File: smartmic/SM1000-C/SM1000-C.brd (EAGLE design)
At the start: 65 x 90 mm, 182 parts, among them CN1 HDR100-3, CN10 MJ-3523-SMT, CN11 HDR100-3, CN12 DF11-16DS, CN2 MOLEX-MINI-B-SMT, CN3 RASM722PX, CN4 RJ-45, CN5 MJ-3523-SMT, CN6 SJ-3524-SMT, CN7 MJ-3523-SMT, CN8 SJ-3524-SMT, CN9 MJ-3523-SMT, J1 JMP-2PIN, J3 JMP-2PIN, J4 JMP-2PIN, J5 JMP-2PIN, P1 TPAD50, P10 TPAD50, P11 TPAD50, P12 TPAD50, P13 TPAD50, P14 TPAD50, P15 TPAD50, P16 TPAD50, P17 TPAD50, P18 TPAD50, P19 TPAD50, P2 TPAD50, P20 TPAD50, P21 PAD070-035, P22 PAD070-035, P23 PAD070-035, P24 PAD070-035, P3 TPAD50, P4 TPAD50, P5 TPAD50, P6 TPAD50, P7 TPAD50, P8 TPAD50, P9 TPAD50, SW1 SW-BOURNS-7914S, SW2 SW-BOURNS-7914S, SW3 DPDT, SW4 SW-BOURNS-7914S, T1 SM-LP-5001, T2 SM-LP-5001, U1 STM32F405, U2 LD3985M33R, U3 STMPS2141, U4 EMIF02-USB03F2, U5 TPS54329E, U6 LMV341, U7 LMV341, U8 LM386M-1, U9 LMV341

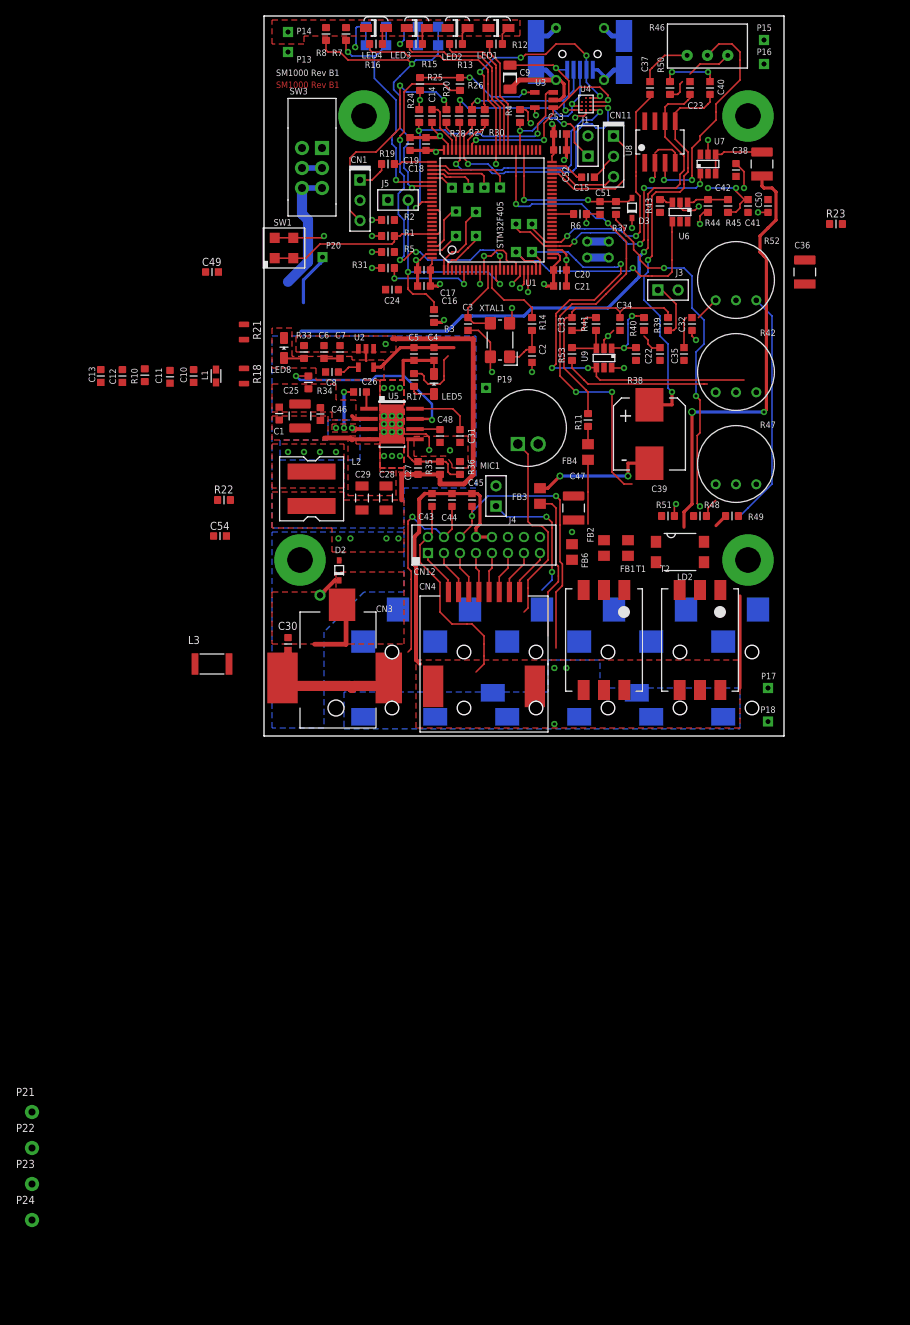
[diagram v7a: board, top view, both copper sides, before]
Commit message: Schematic & PCB changes  RGB 09/24/14
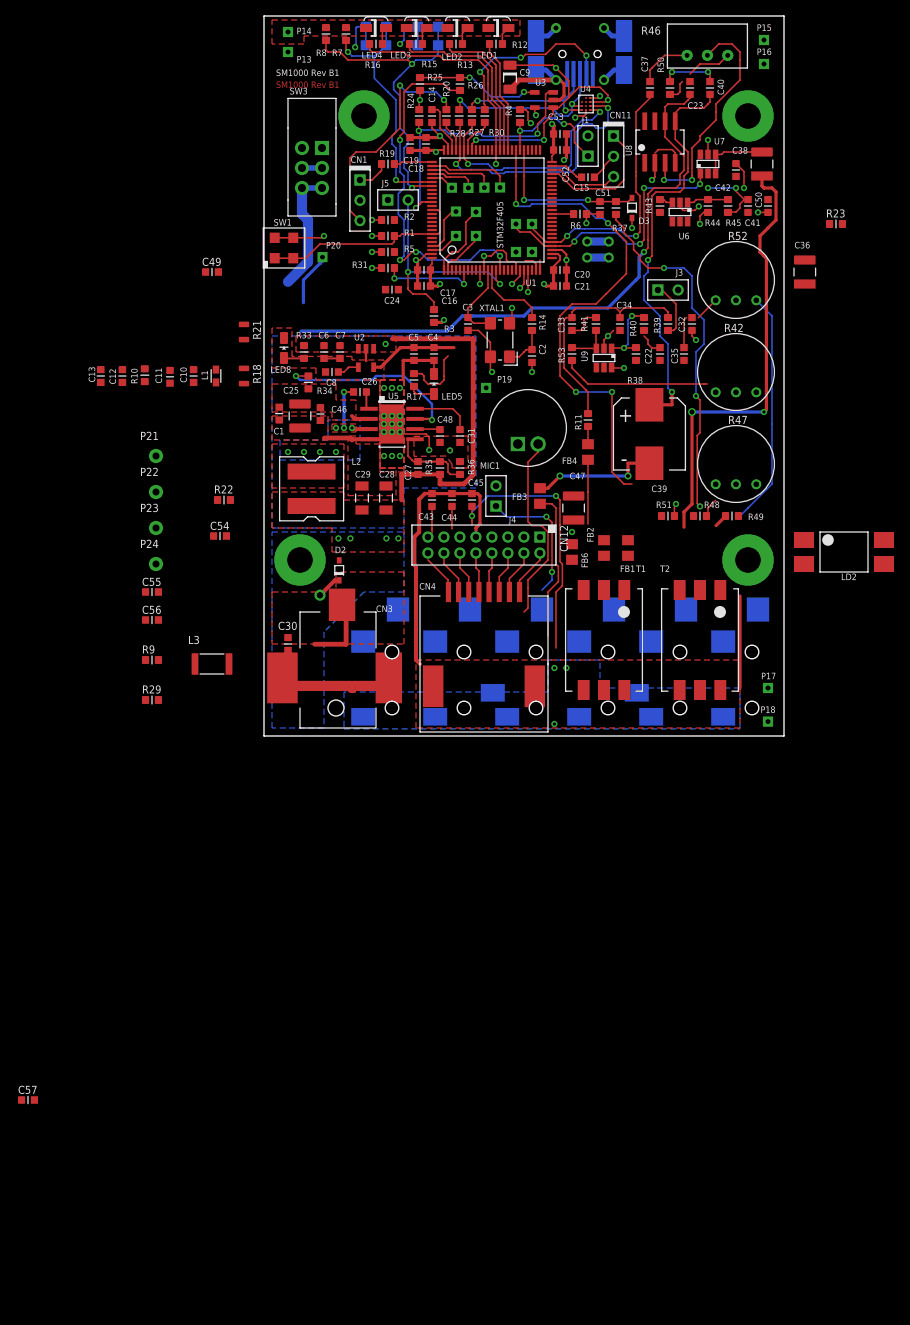
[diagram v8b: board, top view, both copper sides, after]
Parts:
- added C55, C56: 1nF,16V, AA-ipc-7351-capacitor:CAPC1608X92N
- added C57: (no value), AA-ipc-7351-capacitor:CAPC1608X92N
- added R29, R9: 1.5K,1%, AA-ipc-7351-resistor:RESC1608X55N
- CN12: value DF11-16DS -> HRS-DF11-16DS
- LD2: device _RoweTel:SMD4 -> _RoweTel:LTV-817S
- moved P21 83.5 mm to (-13.5, 35.0)
- moved P22 83.5 mm to (-13.5, 30.5)
- moved P23 83.5 mm to (-13.5, 26.0)
- moved P24 83.5 mm to (-13.5, 21.5)
- moved LD2 20.5 mm to (72.5, 23.0)
- turned CN12 to 270 degrees
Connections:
- net !CPPT! renamed !CPTT!
- new net N$27: R23.1, R9.2, U6.4
- new net N$32: C54.2, R29.1, R42.1, U9.4
- net AIN1: now also C56.1, R9.1; no longer R23.1, U6.4
- net AIN2: now also C55.1, R29.2; no longer C54.2, R42.1, U9.4
- net APTT: now also CN12.6; no longer CN12.14
- net AVSS: now also C55.2, C56.2, C57.2
- net MIC: now also CN12.7; no longer CN12.15
- net N$39: now also C57.1
- net N$51: now also CN12.16; no longer CN12.8
- net N$52: now also CN12.15; no longer CN12.7
- net N$53: now also CN12.14; no longer CN12.6
- net N$54: now also CN12.13; no longer CN12.5
- net N$55: now also CN12.12; no longer CN12.4
- net N$56: now also CN12.11; no longer CN12.3
- net N$57: now also CN12.10; no longer CN12.2
- net N$58: now also CN12.9; no longer CN12.1
- net RF: now also CN12.4, CN12.5; no longer CN12.12, CN12.13
- net SPKR: now also CN12.8; no longer CN12.16
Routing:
- net AIN2: track 58.4 -> 1.25 mm, vias 3 -> 0
- net AIN1: track 31.5 -> 2.32 mm, vias 1 -> 0
- net MIC: track 26.7 -> 2.82 mm, vias 1 -> 0
- net SPKR: track 26.6 -> 3.32 mm
- net N$28: track 27.4 -> 25.0 mm
- net APTT: track 35.9 -> 33.8 mm
- net RF: track 49.7 -> 47.7 mm
- net GND: track 127.1 -> 125.3 mm
- net VBUS: track 38.3 -> 37.1 mm
- net N$58: track 5.96 -> 5.10 mm
- net N$23: track 20.1 -> 19.6 mm
- net N$22: track 23.3 -> 22.8 mm
